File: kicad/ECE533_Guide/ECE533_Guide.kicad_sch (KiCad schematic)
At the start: 14 parts, among them J1 DC+, J2 Power_out, J3 DC-, Q3 EPC2304, Q4 EPC2304, Q5 EPC2304, Q6 EPC2304

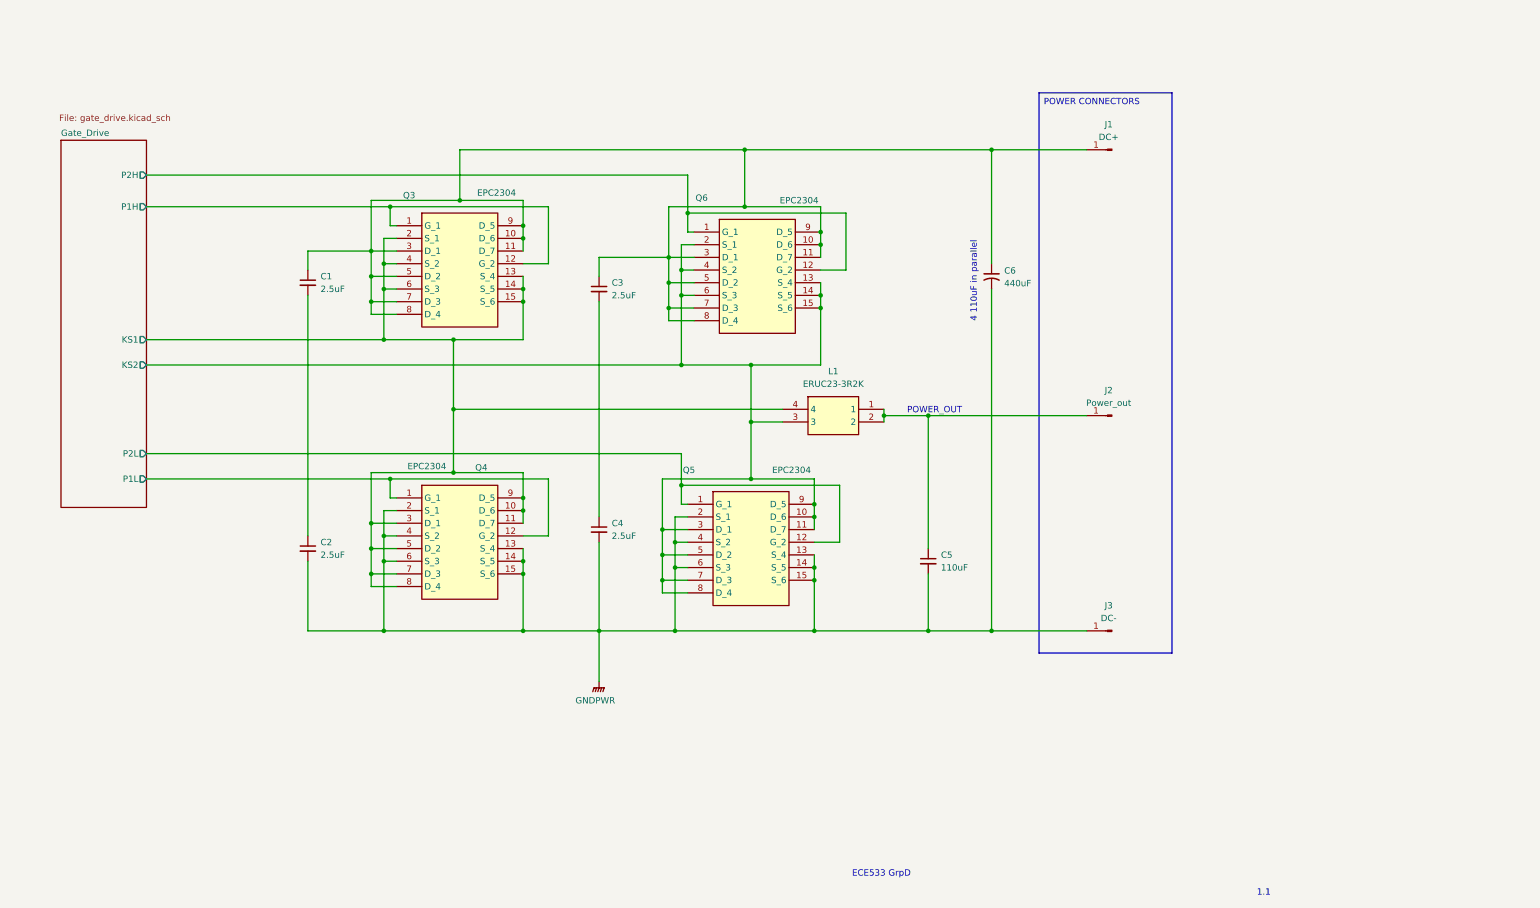
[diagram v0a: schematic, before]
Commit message: Stage 2: hierarchical schematic with isolated control domain (refs #2)
Nine sheets: overview/block diagram, input protection + hot-swap, power
stage with two instances of the phase sheet, aux supply + fan, isolation
barrier crossings, controller and nested fault logic / rack I/O.
Project symbol library ECE533.kicad_sym drawn from manufacturer datasheets.
Replaces the old gate_drive/connectors sheets.

ERC: 0 errors; 11 warnings for custom footprints drawn in Stage 3.
kicad/tools/check_netlist.py: 74/74 connectivity checks pass.

Co-Authored-By: Claude Opus 5.5 <noreply@anthropic.com>
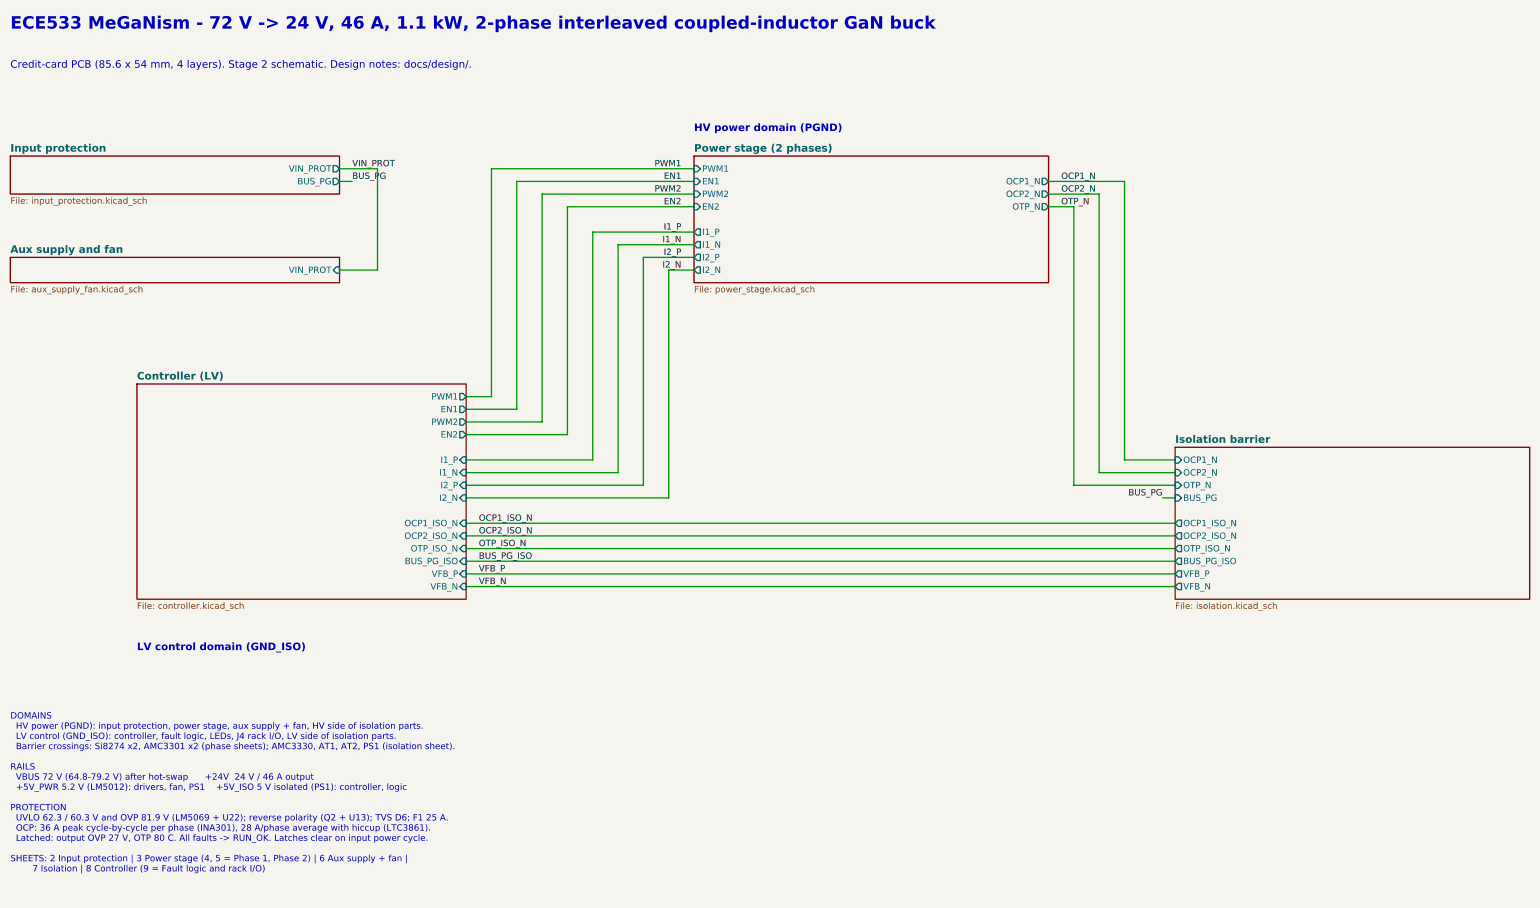
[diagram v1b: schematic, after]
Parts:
- removed C1, C2, C3, C4: 2.5uF, symbol Device:C_Small
- removed C5: 110uF, symbol Device:C_Small
- removed C6: 440uF, symbol Device:C_Small_US
- removed J1: DC+, symbol Connector:Conn_01x01_Pin
- removed J2: Power_out, symbol Connector:Conn_01x01_Pin
- removed J3: DC-, symbol Connector:Conn_01x01_Pin
- removed L1: ERUC23-3R2K, ERUC233R2K, symbol ERUC23-3R2K:ERUC23-3R2K
- removed Q3, Q4, Q5, Q6: EPC2304, EPC2308, symbol EPC2304:EPC2304
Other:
- removed sheet Gate_Drive
- added sheet Aux supply and fan (aux_supply_fan.kicad_sch)
- added sheet Controller (LV) (controller.kicad_sch)
- added sheet Input protection (input_protection.kicad_sch)
- added sheet Isolation barrier (isolation.kicad_sch)
- added sheet Power stage (2 phases) (power_stage.kicad_sch)
- note added: "Credit-card PCB (85.6 x 54 mm, 4 layers). Stage 2 schematic. Design notes: docs/design/."
- note added: "DOMAINS HV power (PGND): input protection, power stage, aux supply + fan, HV side of isolation parts. LV control (GND_ISO): controller, fault logic, LEDs, J4 rack I/O, LV side of isolation parts. Barrier crossings: Si8274 x2, AMC3301 x2 (phase sheets); AMC3330, AT1, AT2, PS1 (isolation sheet). RAILS VBUS 72 V (64.8-79.2 V) after hot-swap +24V 24 V / 46 A output +5V_PWR 5.2 V (LM5012): drivers, fa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"
- note added: "ECE533 MeGaNism - 72 V -> 24 V, 46 A, 1.1 kW, 2-phase interleaved coupled-inductor GaN buck"
- note added: "HV power domain (PGND)"
- note added: "LV control domain (GND_ISO)"
- note removed: "1.1"
- note removed: "4 110uF in parallel"
- note removed: "ECE533 GrpD"
- note removed: "POWER_OUT"
- company: (none) -> ECE533 MeGaNism - 72 V to 24 V 1.1 kW 2-phase GaN buck
- title: (none) -> Overview and block diagram
